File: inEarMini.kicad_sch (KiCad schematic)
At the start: 27 parts, among them J1 Conn_01x02_Pin, J2 Conn_01x02_Pin, J3 Conn_01x02_Pin, SW1 SW_DIP_x01, U1 TL072, U2 TL072, U3 TLE2426xD

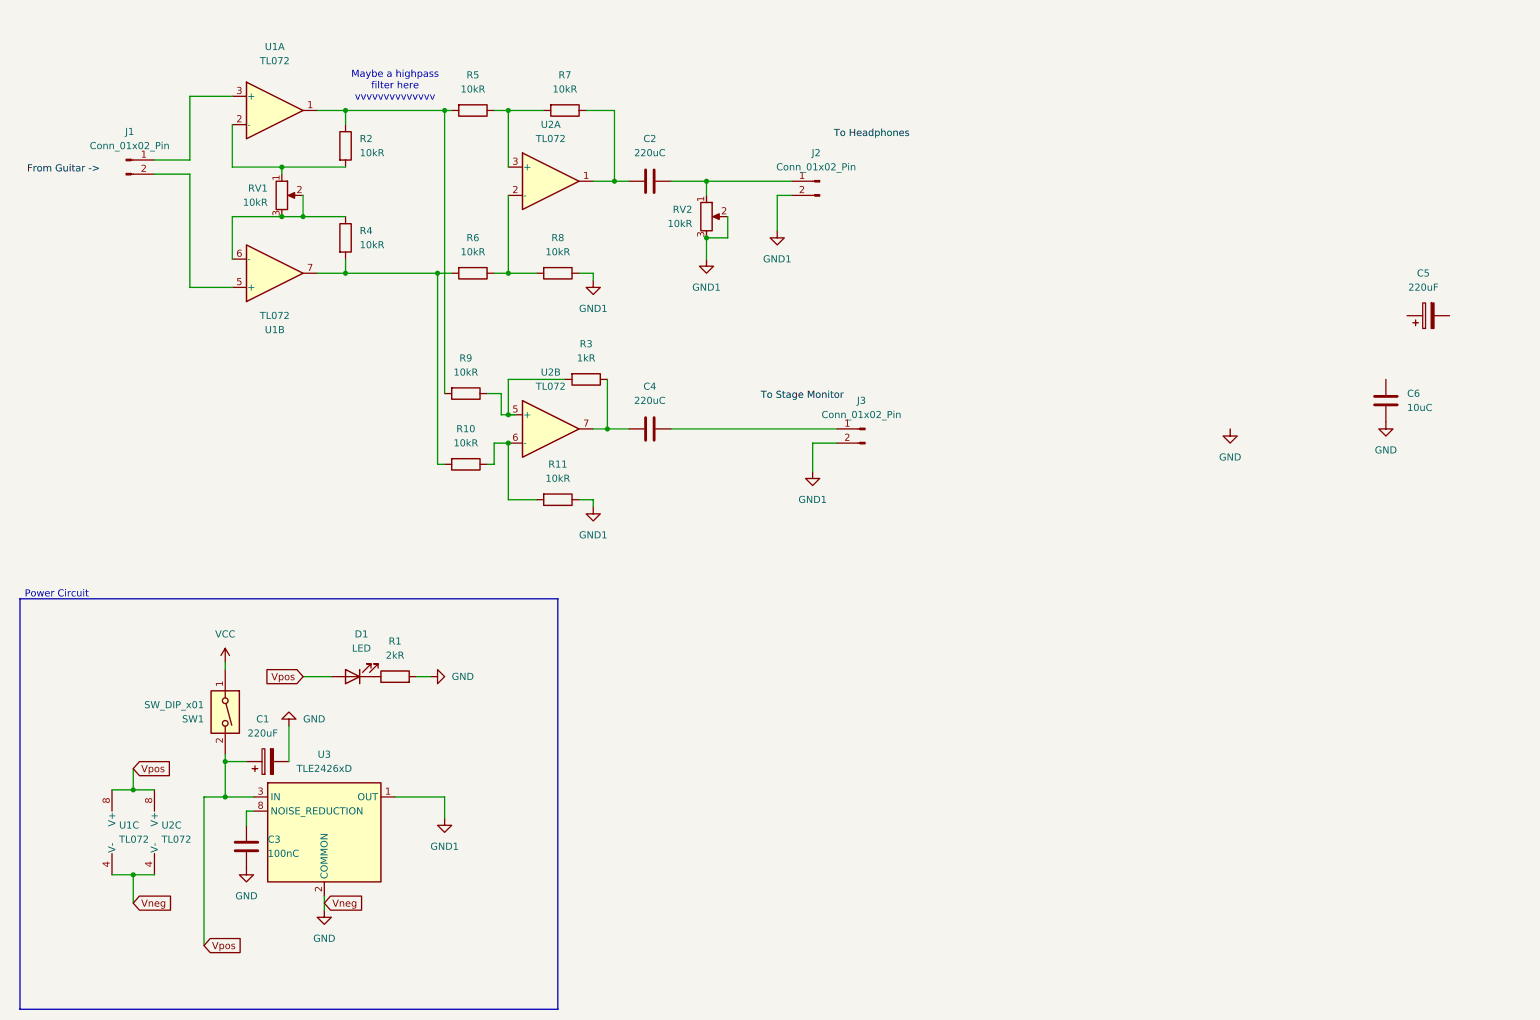
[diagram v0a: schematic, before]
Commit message: Added todos into schematics.
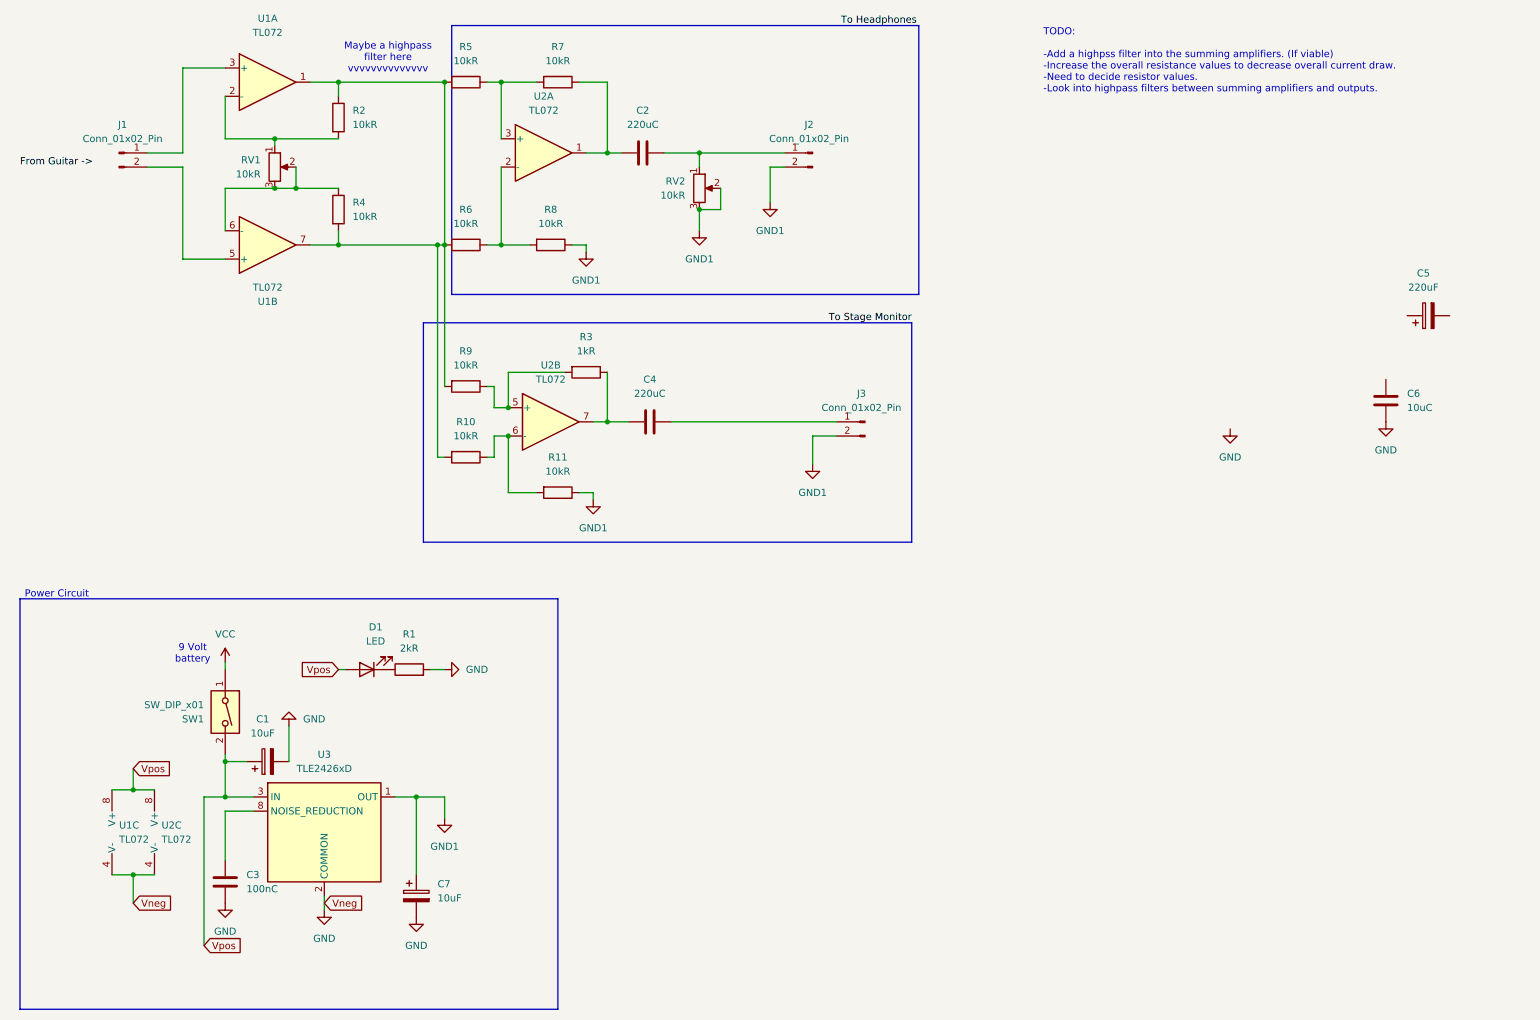
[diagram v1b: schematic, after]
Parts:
- added C7: 10uF, symbol Device:C_Polarized
- C1: value 220uF -> 10uF
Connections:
- net GND: now also C7.2
- net GND1: now also C7.1
- net at R10.2, R4.2, R6.2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: now also R2.1, R5.2, R9.2, U1.1
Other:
- note added: "9 Volt battery"
- note added: "TODO: -Add a highpss filter into the summing amplifiers. (If viable) -Increase the overall resistance values to decrease overall current draw. -Need to decide resistor values. -Look into highpass filters between summing amplifiers and outputs."
- moved on the sheet: C2, C3, C4, D1, J1, J2, J3, R1, R10, R11, R2, R3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
